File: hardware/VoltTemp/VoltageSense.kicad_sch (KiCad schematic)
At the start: 27 parts, among them J14 alert/en_test, J3 psom bms i2c test, J4 bms i2c test, SW1 BMS_BOOT, U1 EL3H7, U2 BQ7692003PW, U3 EL3H7, U4 ISO1641BDR

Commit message: progress
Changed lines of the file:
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@@
+		)
+	)
+	(hierarchical_label "BAT_RTN"
+		(shape passive)
+		(at 34.29 125.73 0)
+		(effects
+			(font
+				(size 1.27 1.27)
+			)
+			(justify left)
 		)
 	)

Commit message: more progress on schematic
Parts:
- removed J3: psom bms i2c test, Connector_PinHeader_2.54mm:PinHeader_1x03_P2.54mm_Vertical, symbol Connector:Conn_01x03_Pin
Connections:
- net at U1.1: now also C1.2, R3.1; no longer R3.2
- net ALERT: now reaches R2.1, U2.20 (ALERT)
- net ALERT: now also R3.2; no longer C1.2, R3.1
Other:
- note added: "BMS Alert"
- note added: "BMS Boot"
- note added: "Either press the button or set bmsEn high to boot the chip"
- note added: "bmsAlert goes high when there is a chip alert"
- note removed: "Various BMS boot methods"
- note removed: "pull alert low"
- moved on the sheet: C1, J4, R1, R10, R2, R3, R9, U1, U4

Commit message: add scrutineering stuff
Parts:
- added R25, R26, R27, R28: 0Ω, Resistor_SMD:R_0805_2012Metric, symbol Device:R
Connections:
- net VC0: now also R25.2
- net VC1: now also R25.1, R26.2
- net VC2: now also R26.1
- net VC3: now also R27.2
- net VC4: now also R27.1, R28.2
- net VC5: now also R28.1
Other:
- note added: "Short cells 3 and 4 to run in a 4 cell configuration"
- moved on the sheet: C1, J4, R1, R10, R3, R5, R9, SW1, U1, U3, U4

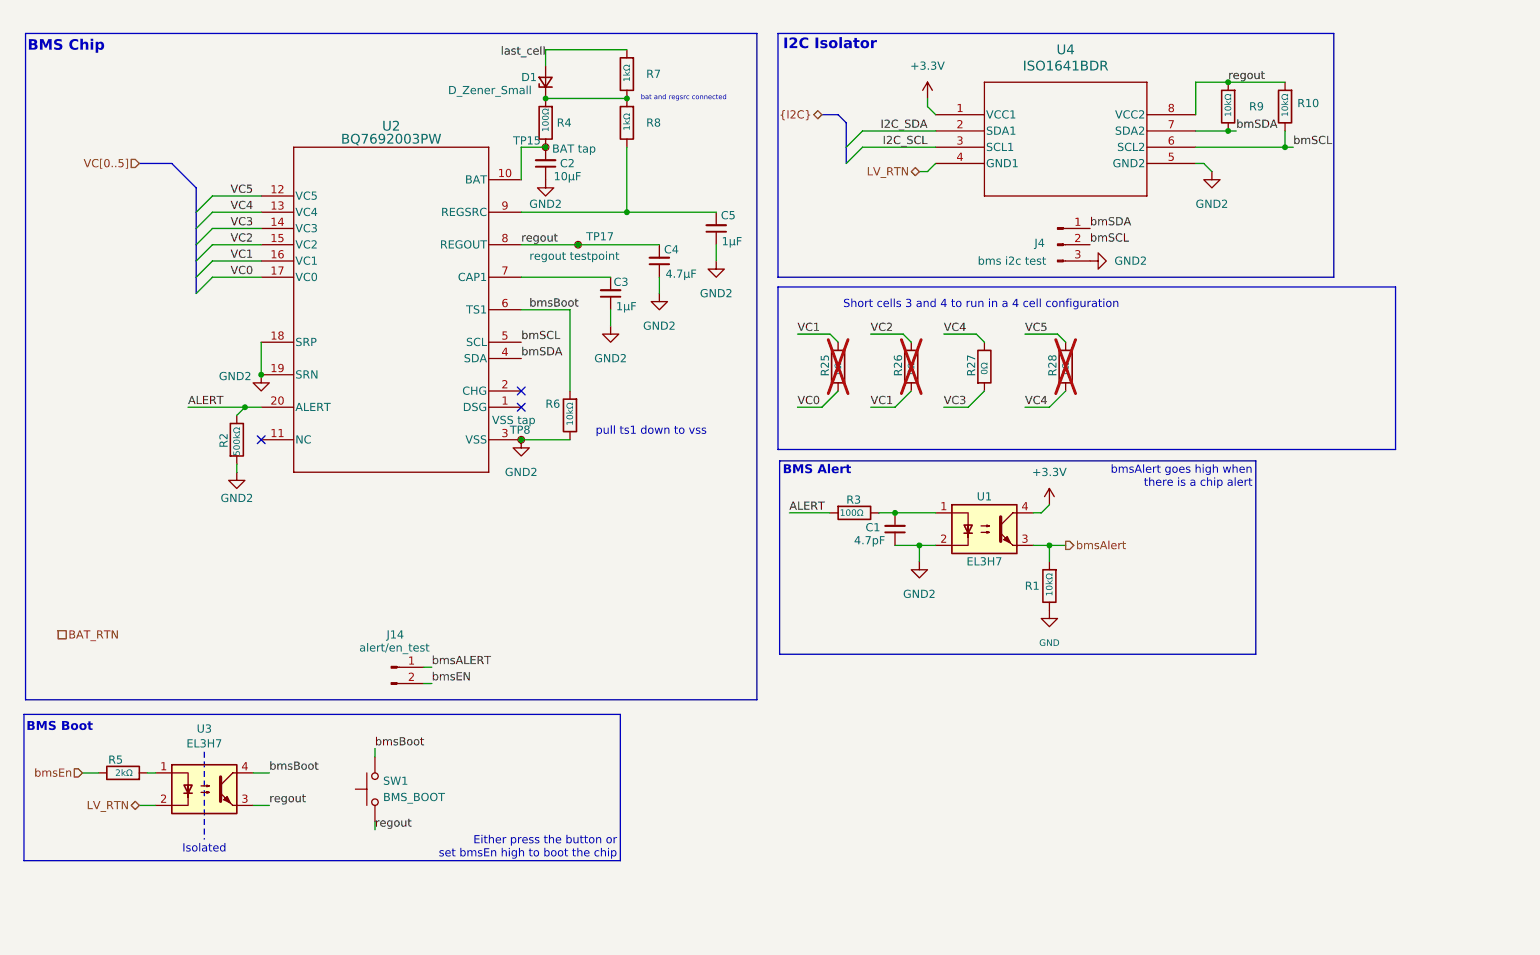
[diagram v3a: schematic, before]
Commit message: clean up schematic a lil bit
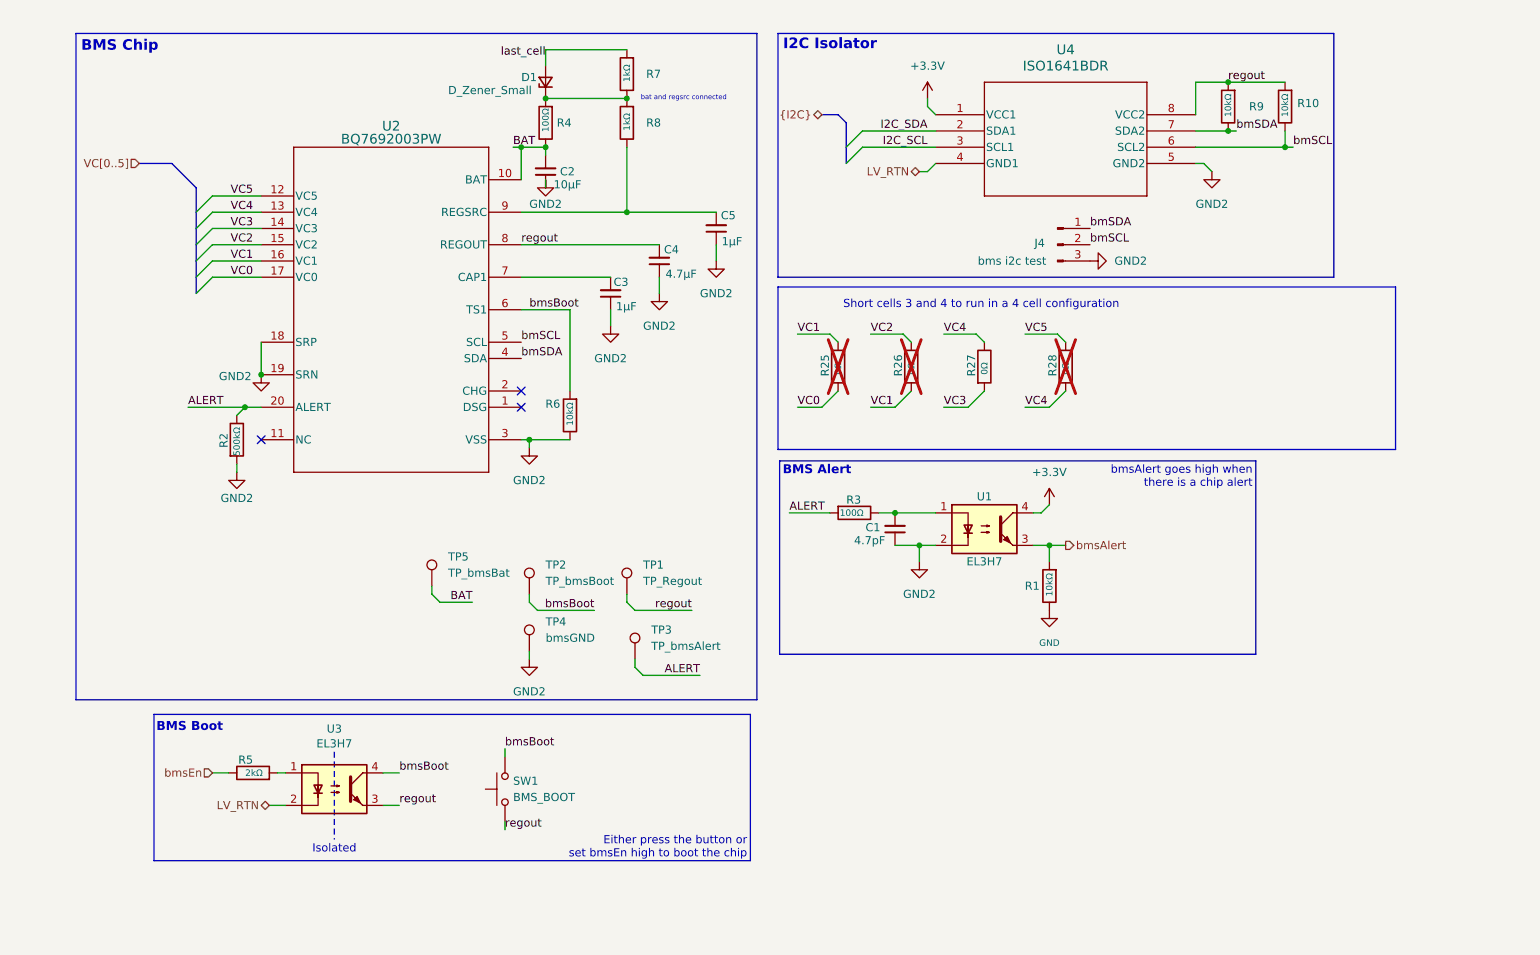
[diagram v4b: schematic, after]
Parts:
- removed J14: alert/en_test, Connector_PinHeader_2.54mm:PinHeader_1x02_P2.54mm_Vertical, symbol Connector:Conn_01x02_Pin
- removed TP15: BAT tap, UTSVT_Special:TestPoint_HEX_3mmID, symbol Connector:TestPoint_Small
- removed TP17: regout testpoint, UTSVT_Special:TestPoint_HEX_3mmID, symbol Connector:TestPoint_Small
- removed TP8: VSS tap, UTSVT_Special:TestPoint_HEX_3mmID, symbol Connector:TestPoint_Small
- added TP1: TP_Regout, symbol Connector:TestPoint
- added TP2: TP_bmsBoot, symbol Connector:TestPoint
- added TP3: TP_bmsAlert, symbol Connector:TestPoint
- added TP4: bmsGND, symbol Connector:TestPoint
- added TP5: TP_bmsBat, symbol Connector:TestPoint
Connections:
- net ALERT: now also TP3.1
- net GND2: now also TP4.1
- net bmsBoot: now also TP2.1
- net regout: now also TP1.1
- net BAT: now reaches C2.2, R4.1, U2.10 (BAT)
- net BAT: now also TP5.1
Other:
- note removed: "pull ts1 down to vss"
- moved on the sheet: C2, R5, SW1, U3
